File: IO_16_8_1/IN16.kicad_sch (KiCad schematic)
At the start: 96 parts, among them J6 Conn_01x06, J7 Conn_01x06, J8 Conn_01x06, Q1 2N7002, Q10 2N7002, Q11 2N7002, Q12 2N7002, Q13 AO3400A, Q14 AO3400A, Q15 AO3400A, Q16 AO3400A, Q17 2N7002, Q18 2N7002, Q19 2N7002, Q2 2N7002, Q20 2N7002, Q21 2N7002, Q22 2N7002, Q23 2N7002, Q24 2N7002, Q3 2N7002, Q4 2N7002, Q5 2N7002, Q6 2N7002, Q7 2N7002, Q8 2N7002, Q9 2N7002

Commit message: changed In_1, In_2
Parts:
- added R98, R99: nmount, Resistor_SMD:R_0603_1608Metric, symbol Device:R
- C28, C29: value 470p -> nmount; now left out of the parts list
- R33, R34, R39, R40: value 10k -> 3k
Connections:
- net +3V3: now also R98.1, R99.1
- net at C28.1, Q1.3 (D), R27.2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: now also R98.2
- net at C29.1, Q2.3 (D), R28.2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: now also R99.2
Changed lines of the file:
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@@
   (junction (at 372.11 39.37) (diameter 0) (color 0 0 0 0)
   )
+  (junction (at 90.17 95.25) (diameter 0) (color 0 0 0 0)
+  )
   (junction (at 105.41 120.65) (diameter 0) (color 0 0 0 0)
   )
@@
   (junction (at 365.76 95.25) (diameter 0) (color 0 0 0 0)
   )
+  (junction (at 90.17 58.42) (diameter 0) (color 0 0 0 0)
+  )
   (junction (at 189.23 170.18) (diameter 0) (color 0 0 0 0)
   )
@@
     (stroke (width 0) (type default) (color 0 0 0 0))
   )
+  (wire (pts (xy 90.17 46.99) (xy 90.17 49.53))
+    (stroke (width 0) (type default) (color 0 0 0 0))
+  )
   (wire (pts (xy 209.55 130.81) (xy 219.71 130.81))
     (stroke (width 0) (type default) (color 0 0 0 0))
@@
     (stroke (width 0) (type default) (color 0 0 0 0))
   )
+  (wire (pts (xy 90.17 57.15) (xy 90.17 58.42))
+    (stroke (width 0) (type default) (color 0 0 0 0))
+  )
   (wire (pts (xy 209.55 198.12) (xy 209.55 199.39))
     (stroke (width 0) (type default) (color 0 0 0 0))
@@
     (stroke (width 0) (type default) (color 0 0 0 0))
   )
-  (wire (pts (xy 85.09 95.25) (xy 92.71 95.25))
+  (wire (pts (xy 85.09 95.25) (xy 90.17 95.25))
     (stroke (width 0) (type default) (color 0 0 0 0))
   )
@@
     (stroke (width 0) (type default) (color 0 0 0 0))
   )
+  (wire (pts (xy 90.17 93.98) (xy 90.17 95.25))
+    (stroke (width 0) (type default) (color 0 0 0 0))
+  )
   (wire (pts (xy 105.41 130.81) (xy 102.87 130.81))
     (stroke (width 0) (type default) (color 0 0 0 0))
@@
     (stroke (width 0) (type default) (color 0 0 0 0))
   )
+  (wire (pts (xy 90.17 58.42) (xy 92.71 58.42))
+    (stroke (width 0) (type default) (color 0 0 0 0))
+  )
   (wire (pts (xy 105.41 248.92) (xy 102.87 248.92))
     (stroke (width 0) (type default) (color 0 0 0 0))
@@
     (stroke (width 0) (type default) (color 0 0 0 0))
   )
+  (wire (pts (xy 90.17 95.25) (xy 92.71 95.25))
+    (stroke (width 0) (type default) (color 0 0 0 0))
+  )
   (wire (pts (xy 209.55 199.39) (xy 209.55 200.66))
     (stroke (width 0) (type default) (color 0 0 0 0))
@@
     (stroke (width 0) (type default) (color 0 0 0 0))
   )
+  (wire (pts (xy 90.17 83.82) (xy 90.17 86.36))
+    (stroke (width 0) (type default) (color 0 0 0 0))
+  )
   (wire (pts (xy 97.79 162.56) (xy 97.79 160.02))
     (stroke (width 0) (type default) (color 0 0 0 0))
@@
     (stroke (width 0) (type default) (color 0 0 0 0))
   )
-  (wire (pts (xy 85.09 58.42) (xy 92.71 58.42))
+  (wire (pts (xy 85.09 58.42) (xy 90.17 58.42))
     (stroke (width 0) (type default) (color 0 0 0 0))
   )
@@
     (pin "1")
   )
+  (symbol (lib_id "Device:R") (at 90.17 53.34 0) (mirror y) (unit 1)
+    (in_bom yes) (on_board yes)
+    (property "Reference" "R98" (id 0) (at 90.17 54.61 90)
+      (effects (font (size 1.27 1.27)) (justify left))
+    )
+    (property "Value" "nmount" (id 1) (at 87.63 55.88 90)
+      (effects (font (size 1.27 1.27)) (justify left))
+    )
+    (property "Footprint" "Resistor_SMD:R_0603_1608Metric" (id 2) (at 91.948 53.34 90)
+      (effects (font (size 1.27 1.27)) hide)
+    )
+    (property "Datasheet" "~" (id 3) (at 90.17 53.34 0)
+      (effects (font (size 1.27 1.27)) hide)
+    )
+    (pin "1")
+    (pin "2")
+  )
   (symbol (lib_id "Transistor_FET:2N7002") (at 358.14 214.63 90) (mirror x) (unit 1)
     (in_bom yes) (on_board yes) (fields_autoplaced)
@@
     (pin "1")
   )
+  (symbol (lib_id "Device:R") (at 90.17 90.17 0) (mirror y) (unit 1)
+    (in_bom yes) (on_board yes)
+    (property "Reference" "R99" (id 0) (at 90.17 91.44 90)
+      (effects (font (size 1.27 1.27)) (justify left))
+    )
+    (property "Value" "nmount" (id 1) (at 87.63 92.71 90)
+      (effects (font (size 1.27 1.27)) (justify left))
+    )
+    (property "Footprint" "Resistor_SMD:R_0603_1608Metric" (id 2) (at 91.948 90.17 90)
+      (effects (font (size 1.27 1.27)) hide)
+    )
+    (property "Datasheet" "~" (id 3) (at 90.17 90.17 0)
+      (effects (font (size 1.27 1.27)) hide)
+    )
+    (pin "1")
+    (pin "2")
+  )
   (symbol (lib_id "Transistor_FET:2N7002") (at 97.79 246.38 90) (mirror x) (unit 1)
     (in_bom yes) (on_board yes) (fields_autoplaced)
@@
       (effects (font (size 1.27 1.27)) (justify left))
     )
-    (property "Value" "10k" (id 1) (at 82.55 92.71 90)
+    (property "Value" "3k" (id 1) (at 82.55 92.71 90)
       (effects (font (size 1.27 1.27)) (justify left))
     )
@@
   )
   (symbol (lib_id "Device:C") (at 85.09 100.33 0) (mirror y) (unit 1)
-    (in_bom yes) (on_board yes)
+    (in_bom no) (on_board yes)
     (property "Reference" "C29" (id 0) (at 86.36 99.06 90)
       (effects (font (size 1.27 1.27)) (justify left))
     )
-    (property "Value" "470p" (id 1) (at 81.28 102.87 90)
+    (property "Value" "nmount" (id 1) (at 81.28 102.87 90)
       (effects (font (size 1.27 1.27)) (justify left))
     )
@@
   )
   (symbol (lib_id "Device:C") (at 85.09 63.5 0) (mirror y) (unit 1)
-    (in_bom yes) (on_board yes)
+    (in_bom no) (on_board yes)
     (property "Reference" "C28" (id 0) (at 86.36 62.23 90)
       (effects (font (size 1.27 1.27)) (justify left))
     )
-    (property "Value" "470p" (id 1) (at 81.28 66.04 90)
+    (property "Value" "nmount" (id 1) (at 81.28 66.04 90)
       (effects (font (size 1.27 1.27)) (justify left))
     )
@@
       (effects (font (size 1.27 1.27)) (justify left))
     )
-    (property "Value" "10k" (id 1) (at 102.87 92.71 90)
+    (property "Value" "3k" (id 1) (at 102.87 92.71 90)
       (effects (font (size 1.27 1.27)) (justify left))
     )
@@
       (effects (font (size 1.27 1.27)) (justify left))
     )
-    (property "Value" "10k" (id 1) (at 102.87 55.88 90)
+    (property "Value" "3k" (id 1) (at 102.87 55.88 90)
       (effects (font (size 1.27 1.27)) (justify left))
     )
@@
     (pin "2")
   )
+  (symbol (lib_id "power:+3V3") (at 90.17 83.82 0) (mirror y) (unit 1)
+    (in_bom yes) (on_board yes)
+    (property "Reference" "#PWR04" (id 0) (at 90.17 87.63 0)
+      (effects (font (size 1.27 1.27)) hide)
+    )
+    (property "Value" "+3V3" (id 1) (at 89.789 79.4258 0))
+    (property "Footprint" "" (id 2) (at 90.17 83.82 0)
+      (effects (font (size 1.27 1.27)) hide)
+    )
+    (property "Datasheet" "" (id 3) (at 90.17 83.82 0)
+      (effects (font (size 1.27 1.27)) hide)
+    )
+    (pin "1")
+  )
   (symbol (lib_id "power:+5V") (at 85.09 158.75 0) (mirror y) (unit 1)
     (in_bom yes) (on_board yes)
@@
     (pin "1")
   )
+  (symbol (lib_id "power:+3V3") (at 90.17 46.99 0) (mirror y) (unit 1)
+    (in_bom yes) (on_board yes)
+    (property "Reference" "#PWR03" (id 0) (at 90.17 50.8 0)
+      (effects (font (size 1.27 1.27)) hide)
+    )
+    (property "Value" "+3V3" (id 1) (at 89.789 42.5958 0))
+    (property "Footprint" "" (id 2) (at 90.17 46.99 0)
+      (effects (font (size 1.27 1.27)) hide)
+    )
+    (property "Datasheet" "" (id 3) (at 90.17 46.99 0)
+      (effects (font (size 1.27 1.27)) hide)
+    )
+    (pin "1")
+  )
   (symbol (lib_id "power:GND") (at 85.09 179.07 0) (mirror y) (unit 1)
     (in_bom yes) (on_board yes)
@@
   (symbol (lib_id "logo:LOGO") (at 307.34 261.62 0) (unit 1)
     (in_bom yes) (on_board yes) (fields_autoplaced)
-    (property "Reference" "#G?" (id 0) (at 307.34 254.7529 0)
+    (property "Reference" "#G2" (id 0) (at 307.34 254.7529 0)
       (effects (font (size 1.27 1.27)) hide)
     )
@@
       (effects (font (size 1.27 1.27)) (justify left))
     )
-    (property "Value" "10k" (id 1) (at 82.55 55.88 90)
+    (property "Value" "3k" (id 1) (at 82.55 55.88 90)
       (effects (font (size 1.27 1.27)) (justify left))
     )

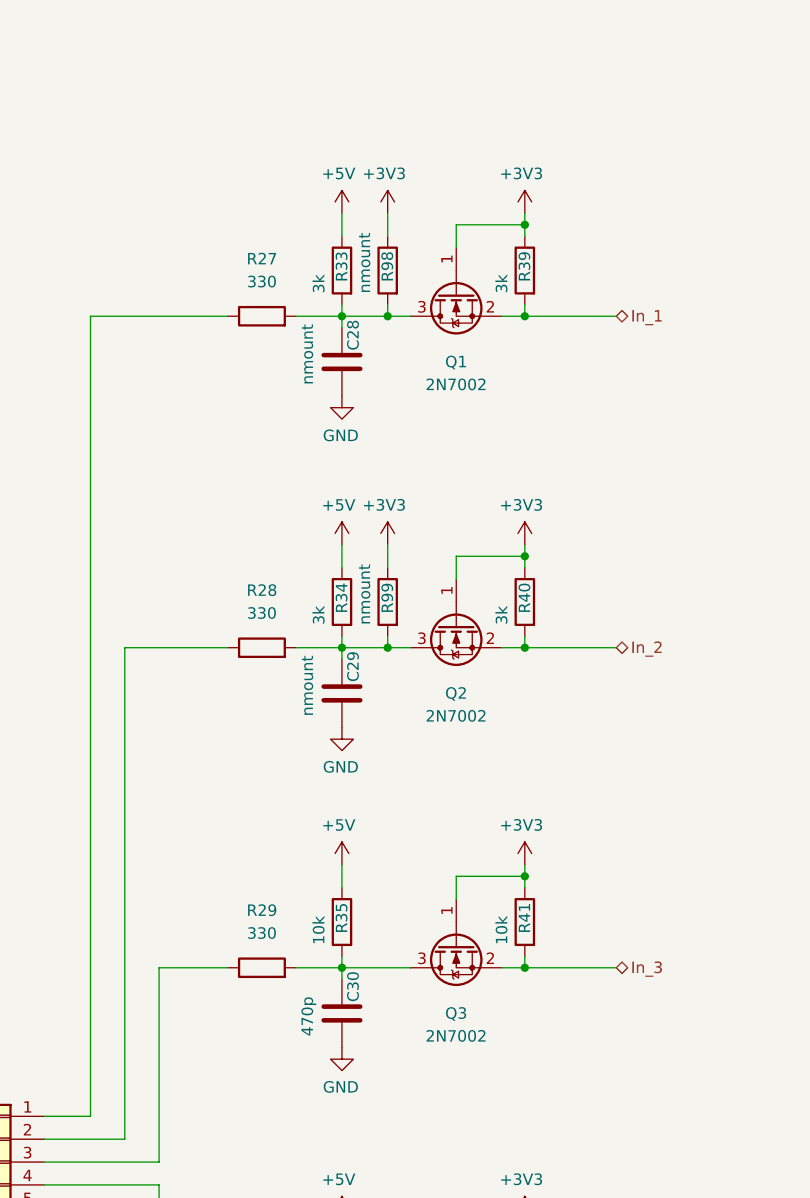
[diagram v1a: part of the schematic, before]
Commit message: different pins for RS485
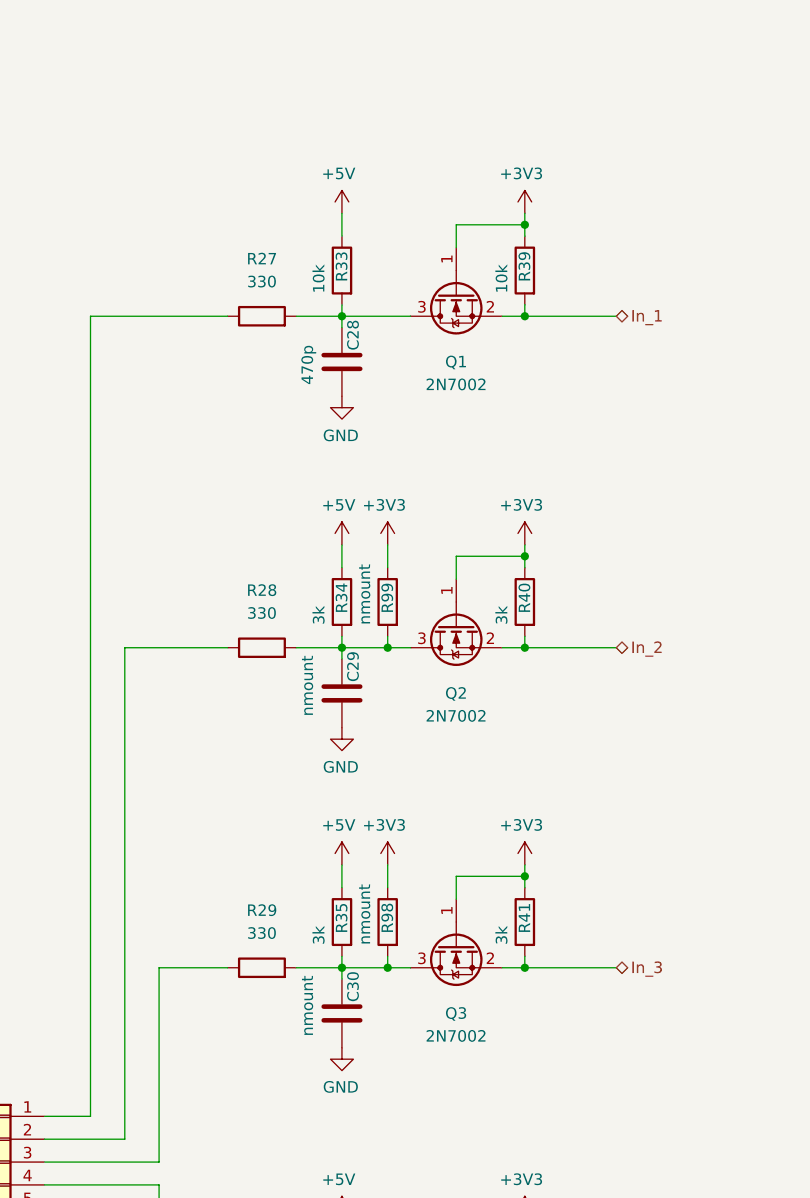
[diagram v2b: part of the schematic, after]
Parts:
- C28: value nmount -> 470p; now in the parts list
- C30: value 470p -> nmount; now left out of the parts list
- R33, R39: value 3k -> 10k
- R35, R41: value 10k -> 3k
- R98, R99: now left out of the parts list
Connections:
- net at C28.1, Q1.3 (D), R27.2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: no longer R98.2
- net at C30.1, Q3.3 (D), R29.2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: now also R98.2
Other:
- moved on the sheet: R98
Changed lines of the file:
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@@
   (junction (at 365.76 95.25) (diameter 0) (color 0 0 0 0)
   )
-  (junction (at 90.17 58.42) (diameter 0) (color 0 0 0 0)
+  (junction (at 90.17 130.81) (diameter 0) (color 0 0 0 0)
   )
   (junction (at 189.23 170.18) (diameter 0) (color 0 0 0 0)
@@
     (stroke (width 0) (type default) (color 0 0 0 0))
   )
-  (wire (pts (xy 90.17 46.99) (xy 90.17 49.53))
+  (wire (pts (xy 90.17 119.38) (xy 90.17 121.92))
     (stroke (width 0) (type default) (color 0 0 0 0))
   )
@@
     (stroke (width 0) (type default) (color 0 0 0 0))
   )
-  (wire (pts (xy 90.17 57.15) (xy 90.17 58.42))
+  (wire (pts (xy 90.17 129.54) (xy 90.17 130.81))
     (stroke (width 0) (type default) (color 0 0 0 0))
   )
@@
     (stroke (width 0) (type default) (color 0 0 0 0))
   )
+  (wire (pts (xy 90.17 130.81) (xy 92.71 130.81))
+    (stroke (width 0) (type default) (color 0 0 0 0))
+  )
   (wire (pts (xy 85.09 132.08) (xy 85.09 130.81))
     (stroke (width 0) (type default) (color 0 0 0 0))
@@
     (stroke (width 0) (type default) (color 0 0 0 0))
   )
-  (wire (pts (xy 90.17 58.42) (xy 92.71 58.42))
+  (wire (pts (xy 85.09 58.42) (xy 92.71 58.42))
     (stroke (width 0) (type default) (color 0 0 0 0))
   )
@@
     (stroke (width 0) (type default) (color 0 0 0 0))
   )
-  (wire (pts (xy 85.09 130.81) (xy 92.71 130.81))
+  (wire (pts (xy 85.09 130.81) (xy 90.17 130.81))
     (stroke (width 0) (type default) (color 0 0 0 0))
   )
@@
     (stroke (width 0) (type default) (color 0 0 0 0))
   )
-  (wire (pts (xy 85.09 58.42) (xy 90.17 58.42))
-    (stroke (width 0) (type default) (color 0 0 0 0))
-  )
   (wire (pts (xy 85.09 248.92) (xy 92.71 248.92))
     (stroke (width 0) (type default) (color 0 0 0 0))
@@
       (effects (font (size 1.27 1.27)) (justify left))
     )
-    (property "Value" "10k" (id 1) (at 102.87 128.27 90)
+    (property "Value" "3k" (id 1) (at 102.87 128.27 90)
       (effects (font (size 1.27 1.27)) (justify left))
     )
@@
     (pin "1")
   )
-  (symbol (lib_id "Device:R") (at 90.17 53.34 0) (mirror y) (unit 1)
-    (in_bom yes) (on_board yes)
-    (property "Reference" "R98" (id 0) (at 90.17 54.61 90)
+  (symbol (lib_id "Device:R") (at 90.17 125.73 0) (mirror y) (unit 1)
+    (in_bom no) (on_board yes)
+    (property "Reference" "R98" (id 0) (at 90.17 127 90)
       (effects (font (size 1.27 1.27)) (justify left))
     )
-    (property "Value" "nmount" (id 1) (at 87.63 55.88 90)
+    (property "Value" "nmount" (id 1) (at 87.63 128.27 90)
       (effects (font (size 1.27 1.27)) (justify left))
     )
-    (property "Footprint" "Resistor_SMD:R_0603_1608Metric" (id 2) (at 91.948 53.34 90)
+    (property "Footprint" "Resistor_SMD:R_0603_1608Metric" (id 2) (at 91.948 125.73 90)
       (effects (font (size 1.27 1.27)) hide)
     )
-    (property "Datasheet" "~" (id 3) (at 90.17 53.34 0)
+    (property "Datasheet" "~" (id 3) (at 90.17 125.73 0)
       (effects (font (size 1.27 1.27)) hide)
     )
@@
   )
   (symbol (lib_id "Device:R") (at 90.17 90.17 0) (mirror y) (unit 1)
-    (in_bom yes) (on_board yes)
+    (in_bom no) (on_board yes)
     (property "Reference" "R99" (id 0) (at 90.17 91.44 90)
       (effects (font (size 1.27 1.27)) (justify left))
@@
   )
   (symbol (lib_id "Device:C") (at 85.09 63.5 0) (mirror y) (unit 1)
-    (in_bom no) (on_board yes)
+    (in_bom yes) (on_board yes)
     (property "Reference" "C28" (id 0) (at 86.36 62.23 90)
       (effects (font (size 1.27 1.27)) (justify left))
     )
-    (property "Value" "nmount" (id 1) (at 81.28 66.04 90)
+    (property "Value" "470p" (id 1) (at 81.28 66.04 90)
       (effects (font (size 1.27 1.27)) (justify left))
     )
@@
       (effects (font (size 1.27 1.27)) (justify left))
     )
-    (property "Value" "3k" (id 1) (at 102.87 55.88 90)
+    (property "Value" "10k" (id 1) (at 102.87 55.88 90)
       (effects (font (size 1.27 1.27)) (justify left))
     )
@@
     (pin "1")
   )
-  (symbol (lib_id "power:+3V3") (at 90.17 46.99 0) (mirror y) (unit 1)
+  (symbol (lib_id "power:+3V3") (at 90.17 119.38 0) (mirror y) (unit 1)
     (in_bom yes) (on_board yes)
-    (property "Reference" "#PWR03" (id 0) (at 90.17 50.8 0)
+    (property "Reference" "#PWR03" (id 0) (at 90.17 123.19 0)
       (effects (font (size 1.27 1.27)) hide)
     )
-    (property "Value" "+3V3" (id 1) (at 89.789 42.5958 0))
-    (property "Footprint" "" (id 2) (at 90.17 46.99 0)
+    (property "Value" "+3V3" (id 1) (at 89.789 114.9858 0))
+    (property "Footprint" "" (id 2) (at 90.17 119.38 0)
       (effects (font (size 1.27 1.27)) hide)
     )
-    (property "Datasheet" "" (id 3) (at 90.17 46.99 0)
+    (property "Datasheet" "" (id 3) (at 90.17 119.38 0)
       (effects (font (size 1.27 1.27)) hide)
     )
@@
   )
   (symbol (lib_id "Device:C") (at 85.09 135.89 0) (mirror y) (unit 1)
-    (in_bom yes) (on_board yes)
+    (in_bom no) (on_board yes)
     (property "Reference" "C30" (id 0) (at 86.36 134.62 90)
       (effects (font (size 1.27 1.27)) (justify left))
     )
-    (property "Value" "470p" (id 1) (at 81.28 138.43 90)
+    (property "Value" "nmount" (id 1) (at 81.28 138.43 90)
       (effects (font (size 1.27 1.27)) (justify left))
     )
@@
       (effects (font (size 1.27 1.27)) (justify left))
     )
-    (property "Value" "3k" (id 1) (at 82.55 55.88 90)
+    (property "Value" "10k" (id 1) (at 82.55 55.88 90)
       (effects (font (size 1.27 1.27)) (justify left))
     )
@@
       (effects (font (size 1.27 1.27)) (justify left))
     )
-    (property "Value" "10k" (id 1) (at 82.55 128.27 90)
+    (property "Value" "3k" (id 1) (at 82.55 128.27 90)
       (effects (font (size 1.27 1.27)) (justify left))
     )

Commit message: PCB init
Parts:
- J6, J7, J8: footprint RTMPin_CAE:Terminal_Block_RTMPin -> IO_16_8_1:Terminal_Block_RTMPin
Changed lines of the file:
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@@
       (effects (font (size 1.27 1.27)) (justify left))
     )
-    (property "Footprint" "RTMPin_CAE:Terminal_Block_RTMPin" (id 2) (at 151.13 152.4 0)
+    (property "Footprint" "IO_16_8_1:Terminal_Block_RTMPin" (id 2) (at 151.13 152.4 0)
       (effects (font (size 1.27 1.27)) hide)
     )
@@
       (effects (font (size 1.27 1.27)) (justify left))
     )
-    (property "Footprint" "RTMPin_CAE:Terminal_Block_RTMPin" (id 2) (at 265.43 152.4 0)
+    (property "Footprint" "IO_16_8_1:Terminal_Block_RTMPin" (id 2) (at 265.43 152.4 0)
       (effects (font (size 1.27 1.27)) hide)
     )
@@
       (effects (font (size 1.27 1.27)) (justify left))
     )
-    (property "Footprint" "RTMPin_CAE:Terminal_Block_RTMPin" (id 2) (at 46.99 152.4 0)
-      (effects (font (size 1.27 1.27)) hide)
-    )
+    (property "Footprint" "IO_16_8_1:Terminal_Block_RTMPin" (id 2) (at 46.99 152.4 0)
+      (effects (font (size 1.27 1.27)) hide)
+    )

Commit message: routed
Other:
- note added: "1"
- note added: "10"
- note added: "11"
- note added: "12"
- note added: "13"
- note added: "14"
- note added: "15"
- note added: "16"
- note added: "2"
- note added: "3"
- note added: "4"
- note added: "5"
- note added: "6"
- note added: "7"
- note added: "8"
- note added: "9"
- note added: "Terminal nr. V"
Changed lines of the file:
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@@
     (stroke (width 0) (type default) (color 0 0 0 0))
+  )
+  (text "5" (at 121.92 212.09 0)
+    (effects (font (size 3 3) (thickness 0.6) bold) (justify left bottom))
+  )
+  (text "2" (at 123.19 97.79 0)
+    (effects (font (size 3 3) (thickness 0.6) bold) (justify left bottom))
+  )
+  (text "9" (at 226.06 133.35 0)
+    (effects (font (size 3 3) (thickness 0.6) bold) (justify left bottom))
+  )
+  (text "11" (at 228.6 212.09 0)
+    (effects (font (size 3 3) (thickness 0.6) bold) (justify left bottom))
+  )
+  (text "14" (at 389.89 97.79 0)
+    (effects (font (size 3 3) (thickness 0.6) bold) (justify left bottom))
+  )
+  (text "15" (at 389.89 158.75 0)
+    (effects (font (size 3 3) (thickness 0.6) bold) (justify left bottom))
   )
   (text "PPUC" (at 316.23 265.43 0)
     (effects (font (size 5 5) bold) (justify left bottom))
   )
+  (text "12" (at 228.6 251.46 0)
+    (effects (font (size 3 3) (thickness 0.6) bold) (justify left bottom))
+  )
+  (text "4" (at 123.19 172.72 0)
+    (effects (font (size 3 3) (thickness 0.6) bold) (justify left bottom))
+  )
+  (text "6" (at 123.19 251.46 0)
+    (effects (font (size 3 3) (thickness 0.6) bold) (justify left bottom))
+  )
+  (text "10" (at 228.6 172.72 0)
+    (effects (font (size 3 3) (thickness 0.6) bold) (justify left bottom))
+  )
+  (text "8" (at 227.33 97.79 0)
+    (effects (font (size 3 3) (thickness 0.6) bold) (justify left bottom))
+  )
+  (text "16" (at 389.89 219.71 0)
+    (effects (font (size 3 3) (thickness 0.6) bold) (justify left bottom))
+  )
+  (text "3" (at 123.19 133.35 0)
+    (effects (font (size 3 3) (thickness 0.6) bold) (justify left bottom))
+  )
+  (text "Terminal nr.\n    V" (at 120.65 54.61 0)
+    (effects (font (size 1.27 1.27)) (justify left bottom))
+  )
+  (text "7" (at 226.06 60.96 0)
+    (effects (font (size 3 3) (thickness 0.6) bold) (justify left bottom))
+  )
+  (text "13" (at 389.89 41.91 0)
+    (effects (font (size 3 3) (thickness 0.6) bold) (justify left bottom))
+  )
+  (text "1" (at 123.19 60.96 0)
+    (effects (font (size 3 3) (thickness 0.6) bold) (justify left bottom))
+  )
   (hierarchical_label "In_15" (shape bidirectional) (at 381 156.21 0)
